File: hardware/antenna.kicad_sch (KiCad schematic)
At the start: 9 parts

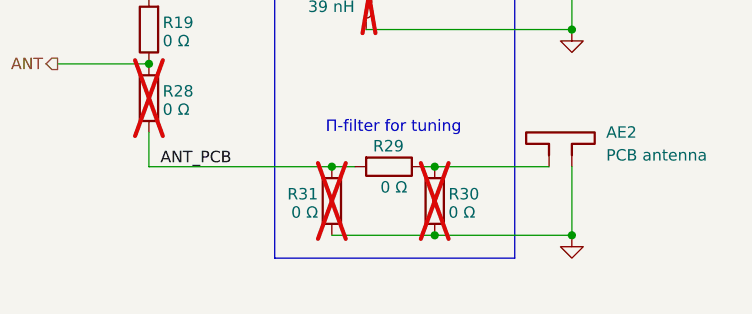
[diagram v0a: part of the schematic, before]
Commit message: HW: Add layout guidelines/reminders to schematic
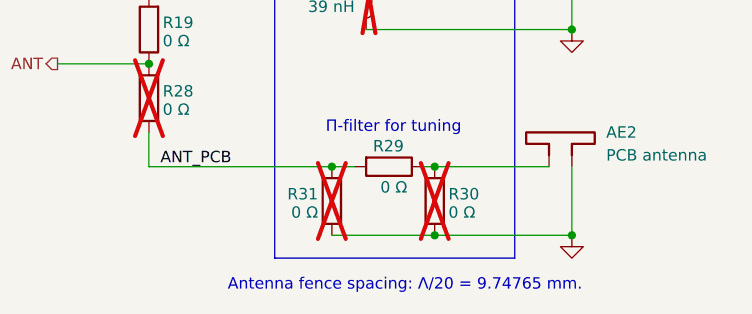
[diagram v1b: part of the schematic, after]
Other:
- note added: "Antenna fence spacing: Λ/20 = 9.74765 mm."
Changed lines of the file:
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@@
+		)
+	)
+	(text "Antenna fence spacing: Λ/20 = 9.74765 mm."
+		(exclude_from_sim no)
+		(at 131.318 124.968 0)
+		(effects
+			(font
+				(size 1.27 1.27)
+			)
 		)
 	)

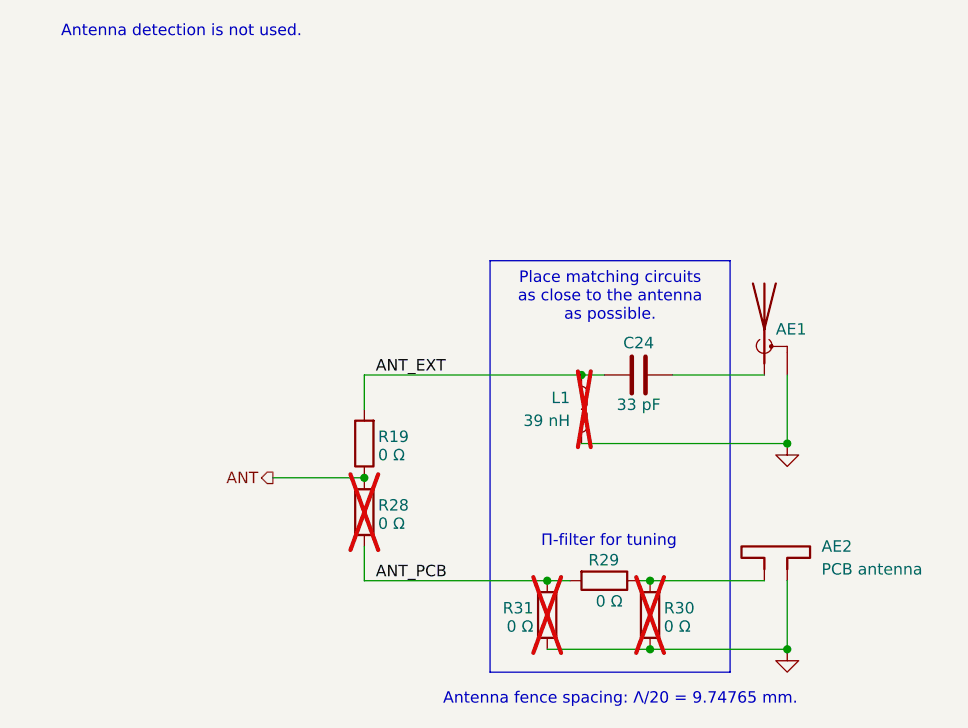
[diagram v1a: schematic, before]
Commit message: HW: Cleanup schematic
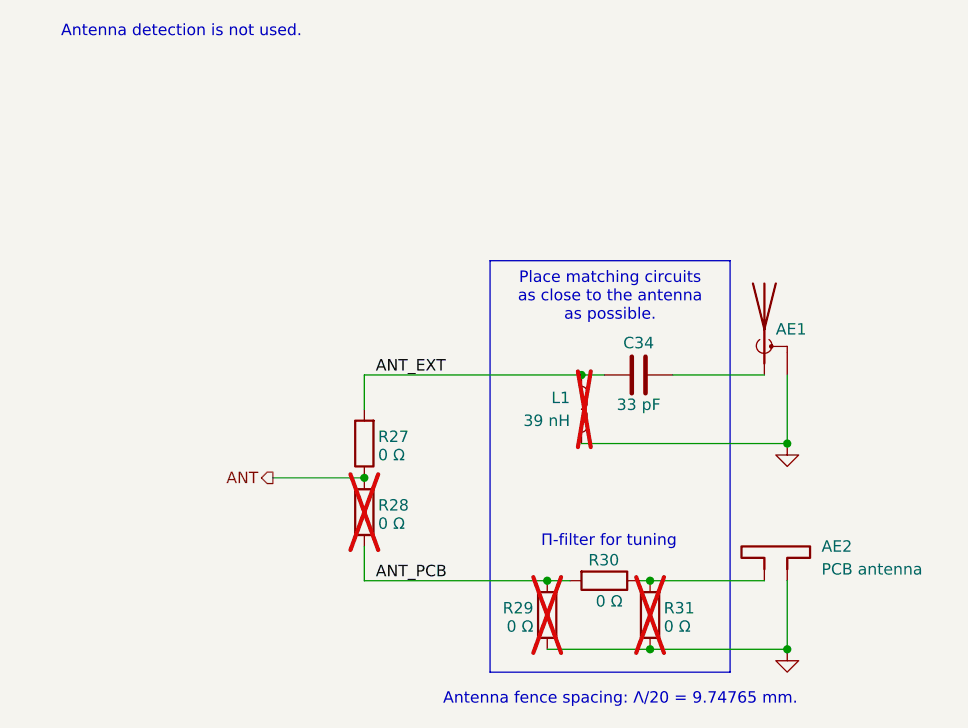
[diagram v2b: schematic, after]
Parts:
- renumbered C24 to C34, R19 to R27, R31 to R29, R29 to R30, R30 to R31
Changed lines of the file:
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@@
 		(on_board yes)
 		(dnp no)
-		(property "Reference" "C24"
+		(property "Reference" "C34"
 			(at 133.35 85.344 90)
 			(effects
@@
 			(project "iida_devkit"
 				(path "/b12a6e25-97fb-4aba-bc96-af8db389bb9a/6e456e95-dbda-43fc-b148-815c3be21ba0"
-					(reference "C24")
+					(reference "C34")
 					(unit 1)
 				)
@@
 		(on_board yes)
 		(dnp no)
-		(property "Reference" "R19"
+		(property "Reference" "R27"
 			(at 104.394 95.758 0)
 			(effects
@@
 			(project "iida_devkit"
 				(path "/b12a6e25-97fb-4aba-bc96-af8db389bb9a/6e456e95-dbda-43fc-b148-815c3be21ba0"
-					(reference "R19")
+					(reference "R27")
 					(unit 1)
 				)
@@
 		(on_board yes)
 		(dnp no)
-		(property "Reference" "R29"
+		(property "Reference" "R30"
 			(at 127.762 109.474 90)
 			(effects
@@
 			(project "iida_devkit"
 				(path "/b12a6e25-97fb-4aba-bc96-af8db389bb9a/6e456e95-dbda-43fc-b148-815c3be21ba0"
-					(reference "R29")
+					(reference "R30")
 					(unit 1)
 				)
@@
 		(dnp no)
 		(fields_autoplaced yes)
-		(property "Reference" "#PWR019"
+		(property "Reference" "#PWR026"
 			(at 149.86 125.73 0)
 			(effects
@@
 			(project "iida_devkit"
 				(path "/b12a6e25-97fb-4aba-bc96-af8db389bb9a/6e456e95-dbda-43fc-b148-815c3be21ba0"
-					(reference "#PWR019")
+					(reference "#PWR026")
 					(unit 1)
 				)
@@
 		(on_board yes)
 		(dnp yes)
-		(property "Reference" "R31"
+		(property "Reference" "R29"
 			(at 121.666 114.808 0)
 			(effects
@@
 			(project "iida_devkit"
 				(path "/b12a6e25-97fb-4aba-bc96-af8db389bb9a/6e456e95-dbda-43fc-b148-815c3be21ba0"
-					(reference "R31")
+					(reference "R29")
 					(unit 1)
 				)
@@
 		(on_board yes)
 		(dnp yes)
-		(property "Reference" "R30"
+		(property "Reference" "R31"
 			(at 136.144 114.808 0)
 			(effects
@@
 			(project "iida_devkit"
 				(path "/b12a6e25-97fb-4aba-bc96-af8db389bb9a/6e456e95-dbda-43fc-b148-815c3be21ba0"
-					(reference "R30")
+					(reference "R31")
 					(unit 1)
 				)
@@
 		(dnp no)
 		(fields_autoplaced yes)
-		(property "Reference" "#PWR018"
+		(property "Reference" "#PWR025"
 			(at 149.86 102.87 0)
 			(effects
@@
 			(project "iida_devkit"
 				(path "/b12a6e25-97fb-4aba-bc96-af8db389bb9a/6e456e95-dbda-43fc-b148-815c3be21ba0"
-					(reference "#PWR018")
-					(unit 1)
-				)
+					(reference "#PWR025")
+					(unit 1)
+				)

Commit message: HW: Fix PCB antenna
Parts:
- AE2: footprint PCB_antenna:800MHz_inverted_f_antenna -> PCB_antenna:800MHz_antenna
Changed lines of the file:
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@@
 			)
 		)
-		(property "Footprint" "PCB_antenna:800MHz_inverted_f_antenna"
+		(property "Footprint" "PCB_antenna:800MHz_antenna"
 			(at 147.32 106.68 0)
 			(effects

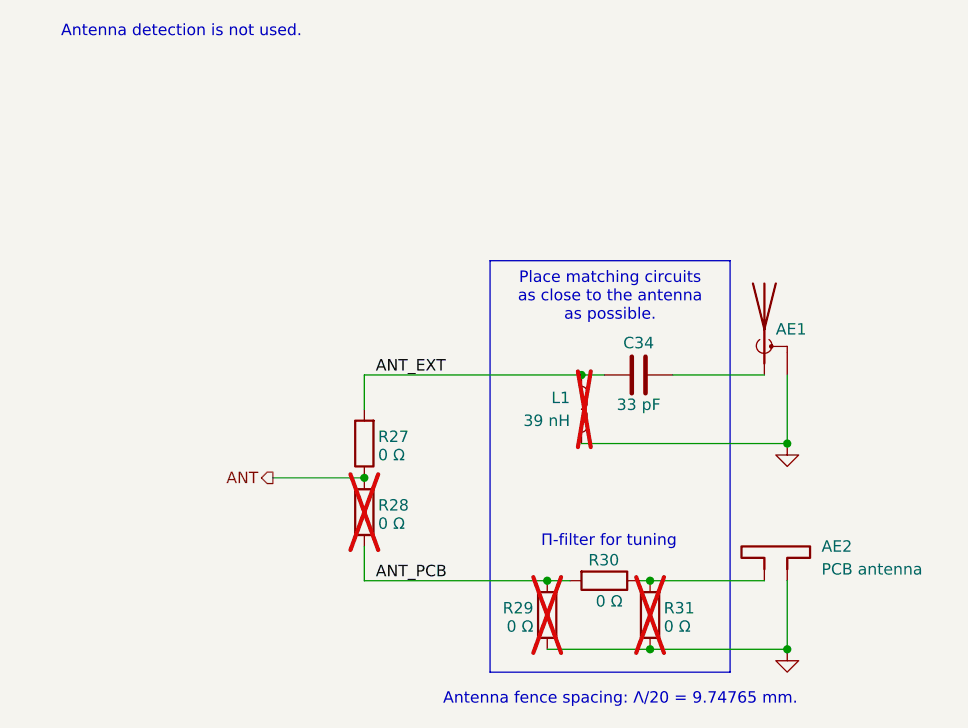
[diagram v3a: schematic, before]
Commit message: HW: Add series termination to UART lines
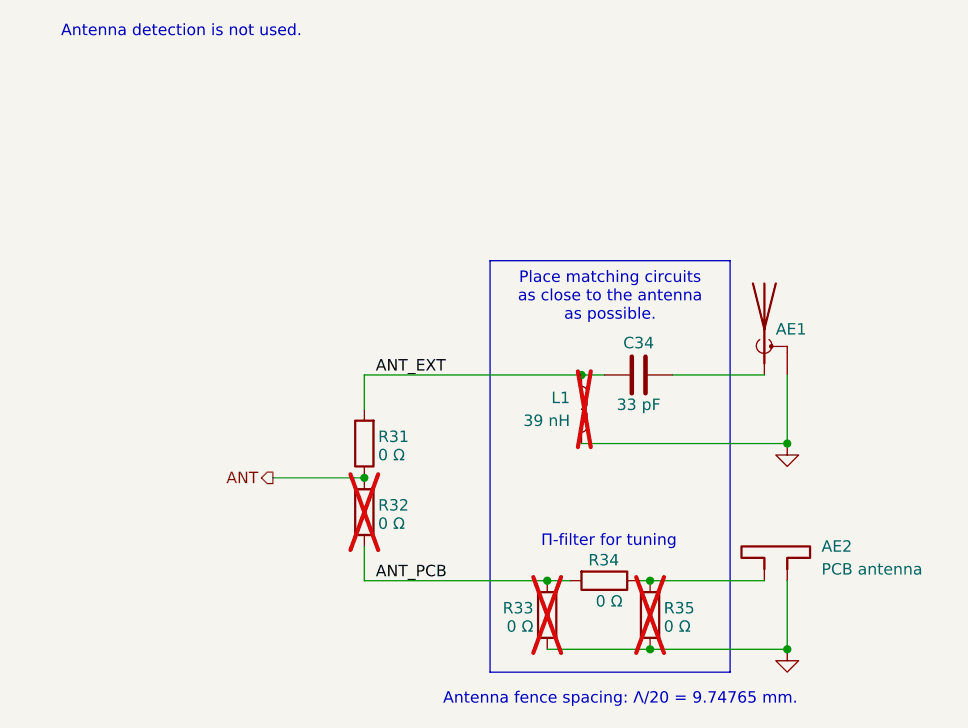
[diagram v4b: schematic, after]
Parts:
- renumbered R27 to R31, R28 to R32, R29 to R33, R30 to R34, R31 to R35
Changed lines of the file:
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@@
 		(on_board yes)
 		(dnp no)
-		(property "Reference" "R27"
+		(property "Reference" "R31"
 			(at 104.394 95.758 0)
 			(effects
@@
 			(project "iida_devkit"
 				(path "/b12a6e25-97fb-4aba-bc96-af8db389bb9a/6e456e95-dbda-43fc-b148-815c3be21ba0"
-					(reference "R27")
+					(reference "R31")
 					(unit 1)
 				)
@@
 		(on_board yes)
 		(dnp no)
-		(property "Reference" "R30"
+		(property "Reference" "R34"
 			(at 127.762 109.474 90)
 			(effects
@@
 			(project "iida_devkit"
 				(path "/b12a6e25-97fb-4aba-bc96-af8db389bb9a/6e456e95-dbda-43fc-b148-815c3be21ba0"
-					(reference "R30")
+					(reference "R34")
 					(unit 1)
 				)
@@
 		(on_board yes)
 		(dnp yes)
-		(property "Reference" "R29"
+		(property "Reference" "R33"
 			(at 121.666 114.808 0)
 			(effects
@@
 			(project "iida_devkit"
 				(path "/b12a6e25-97fb-4aba-bc96-af8db389bb9a/6e456e95-dbda-43fc-b148-815c3be21ba0"
-					(reference "R29")
+					(reference "R33")
 					(unit 1)
 				)
@@
 		(on_board yes)
 		(dnp yes)
-		(property "Reference" "R31"
+		(property "Reference" "R35"
 			(at 136.144 114.808 0)
 			(effects
@@
 			(project "iida_devkit"
 				(path "/b12a6e25-97fb-4aba-bc96-af8db389bb9a/6e456e95-dbda-43fc-b148-815c3be21ba0"
-					(reference "R31")
+					(reference "R35")
 					(unit 1)
 				)
@@
 		(on_board yes)
 		(dnp yes)
-		(property "Reference" "R28"
+		(property "Reference" "R32"
 			(at 104.394 103.378 0)
 			(effects
@@
 			(project "iida_devkit"
 				(path "/b12a6e25-97fb-4aba-bc96-af8db389bb9a/6e456e95-dbda-43fc-b148-815c3be21ba0"
-					(reference "R28")
-					(unit 1)
-				)
+					(reference "R32")
+					(unit 1)
+				)

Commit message: HW: Layout antenna
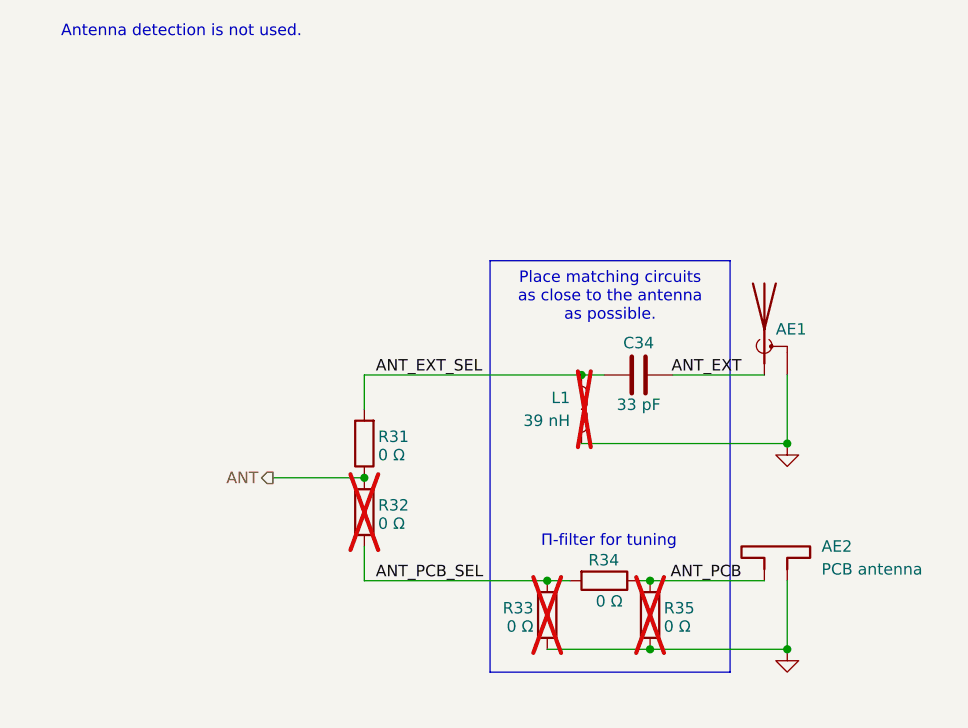
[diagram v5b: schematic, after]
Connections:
- net ANT_EXT: now also AE1.1 (A), C34.1; no longer C34.2, L1.1, R31.2
- net ANT_PCB: now also AE2.1, R34.1, R35.2; no longer R32.1, R33.2, R34.2
- new net ANT_EXT_SEL: C34.2, L1.1, R31.2
- new net ANT_PCB_SEL: R32.1, R33.2, R34.2
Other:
- note removed: "Antenna fence spacing: Λ/20 = 9.74765 mm."
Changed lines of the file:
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@@
-		)
-	)
-	(text "Antenna fence spacing: Λ/20 = 9.74765 mm."
-		(exclude_from_sim no)
-		(at 131.318 124.968 0)
-		(effects
-			(font
-				(size 1.27 1.27)
-			)
 		)
 	)
@@
 		)
 	)
-	(label "ANT_PCB"
+	(label "ANT_PCB_SEL"
 		(at 104.14 111.76 0)
 		(fields_autoplaced yes)
@@
 	)
 	(label "ANT_EXT"
+		(at 144.78 88.9 180)
+		(fields_autoplaced yes)
+		(effects
+			(font
+				(size 1.27 1.27)
+			)
+			(justify right bottom)
+		)
+	)
+	(label "ANT_PCB"
+		(at 144.78 111.76 180)
+		(fields_autoplaced yes)
+		(effects
+			(font
+				(size 1.27 1.27)
+			)
+			(justify right bottom)
+		)
+	)
+	(label "ANT_EXT_SEL"
 		(at 104.14 88.9 0)
 		(fields_autoplaced yes)

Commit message: HW: Connect signals
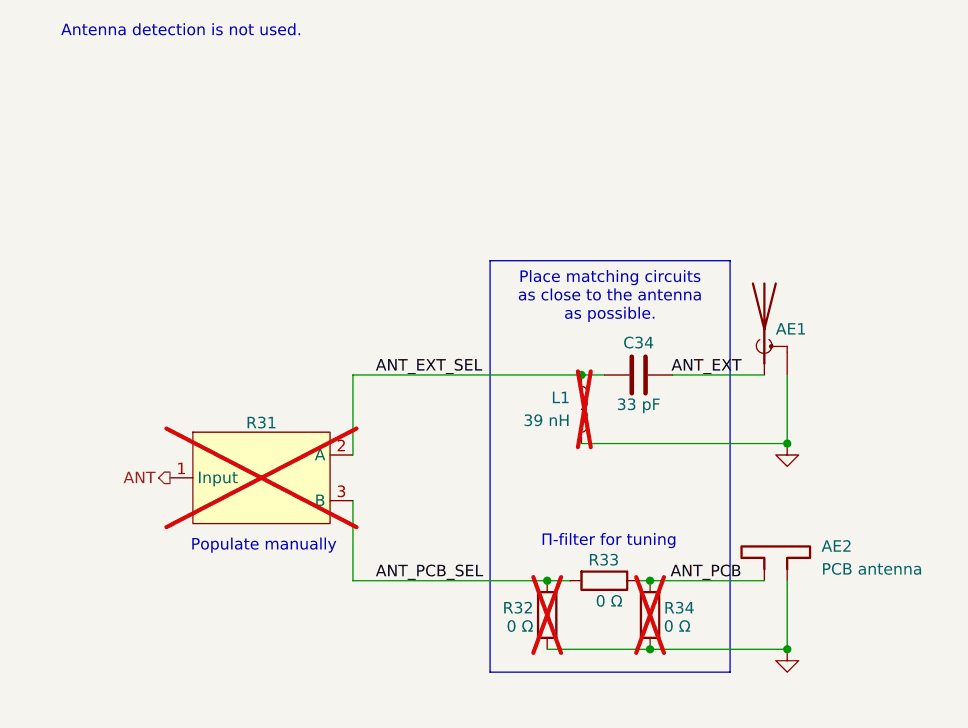
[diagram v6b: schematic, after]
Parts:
- removed R31, R32: 0 Ω, perfect_footprints:0402_1005_perfect, symbol Device:R
- added R31: ~, perfect_footprints:0hm_choice, symbol perfect_footprints:0hm_choice
- renumbered R33 to R32, R34 to R33, R35 to R34
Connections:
- net ANT: now also R31.1 (Input)
- net ANT_EXT_SEL: now also R31.2 (A)
- net ANT_PCB_SEL: now also R31.3 (B)
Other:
- note added: "Populate manually"

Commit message: HW: Finish layout
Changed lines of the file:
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@@
 	(title_block
 		(title "Iida devkit")
-		(date "2024-09-10")
-		(rev "v4.0.0")
+		(date "2024-09-21")
+		(rev "v4.1.0")
 	)
 	(junction
@@
 	)
 	(junction
-		(at 149.86 119.38)
+		(at 134.62 111.76)
 		(diameter 0)
 		(color 0 0 0 0)
 	)
 	(junction
-		(at 134.62 111.76)
+		(at 149.86 119.38)
 		(diameter 0)
 		(color 0 0 0 0)
@@
 	(wire
 		(pts
+			(xy 149.86 111.76) (xy 149.86 119.38)
+		)
+		(stroke
+			(width 0)
+			(type default)
+		)
+	)
+	(wire
+		(pts
 			(xy 101.6 97.79) (xy 101.6 88.9)
 		)
@@
 		)
 	)
-	(wire
-		(pts
-			(xy 149.86 111.76) (xy 149.86 119.38)
-		)
-		(stroke
-			(width 0)
-			(type default)
-		)
-	)
 	(image
 		(at 237.49 118.11)
@@
 		(dnp no)
 		(property "Reference" "AE2"
-			(at 153.67 107.9499 0)
+			(at 146.558 104.648 0)
 			(effects
 				(font
@@
 		)
 		(property "Value" "PCB antenna"
-			(at 153.67 110.4899 0)
+			(at 144.272 106.68 0)
 			(effects
 				(font
